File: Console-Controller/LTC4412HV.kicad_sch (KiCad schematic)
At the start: 5 parts, among them Q5 Si7463DP, U11 LTC4412HVIS6

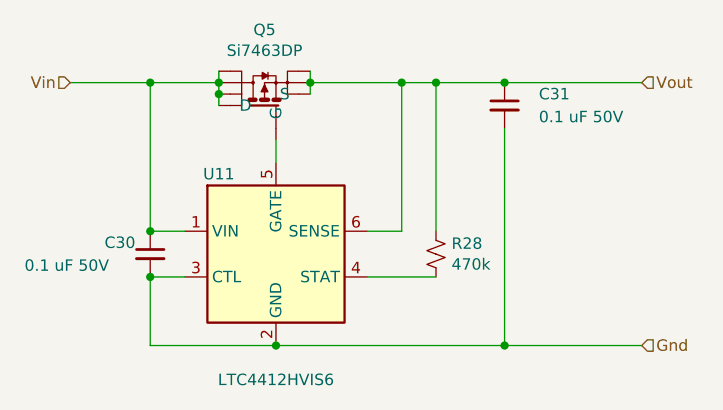
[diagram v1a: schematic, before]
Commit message: added polyfuse to LTC1760 output
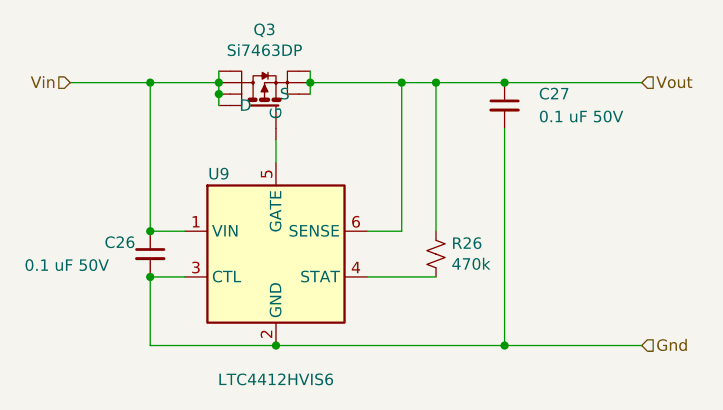
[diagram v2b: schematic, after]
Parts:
- renumbered C30 to C26, C31 to C27, Q5 to Q3, R28 to R26, U11 to U9
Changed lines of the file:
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@@
   (symbol (lib_id "Power_Management:LTC4412xS6") (at 140.97 101.6 0)
     (in_bom yes) (on_board yes)
-    (property "Reference" "U11" (id 0) (at 134.62 92.71 0))
+    (property "Reference" "U9" (id 0) (at 134.62 92.71 0))
     (property "Value" "LTC4412HVIS6" (id 1) (at 140.97 115.57 0))
     (property "Footprint" "Package_TO_SOT_SMD:TSOT-23-6" (id 2) (at 157.48 110.49 0)
@@
   (symbol (lib_id "ProjectDevices:Si7463DP") (at 139.7 82.55 270) (mirror x)
     (in_bom yes) (on_board yes)
-    (property "Reference" "Q5" (id 0) (at 139.7 76.6826 90))
+    (property "Reference" "Q3" (id 0) (at 139.7 76.6826 90))
     (property "Value" "Si7463DP" (id 1) (at 139.7 78.994 90))
     (property "Footprint" "Package_SO:PowerPAK_SO-8_Single" (id 2) (at 139.7 82.55 0)
@@
   (symbol (lib_id "Device:C_Small") (at 127 101.6 0)
     (in_bom yes) (on_board yes)
-    (property "Reference" "C30" (id 0) (at 121.92 100.33 0)
+    (property "Reference" "C26" (id 0) (at 121.92 100.33 0)
       (effects (font (size 1.27 1.27)) (justify left))
     )
@@
   (symbol (lib_id "Device:C_Small") (at 166.37 85.09 0)
     (in_bom yes) (on_board yes)
-    (property "Reference" "C31" (id 0) (at 170.18 83.82 0)
+    (property "Reference" "C27" (id 0) (at 170.18 83.82 0)
       (effects (font (size 1.27 1.27)) (justify left))
     )
@@
   (symbol (lib_id "Device:R_Small_US") (at 158.75 101.6 0)
     (in_bom yes) (on_board yes)
-    (property "Reference" "R28" (id 0) (at 160.4772 100.4316 0)
+    (property "Reference" "R26" (id 0) (at 160.4772 100.4316 0)
       (effects (font (size 1.27 1.27)) (justify left))
     )

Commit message: latest WIP, LTC1760 module ready for layout, strone-controller ready for layout but needs mech board drawings
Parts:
- renumbered C26 to C?, C27 to C?, Q3 to Q?, R26 to R?, U9 to U?
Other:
- company: Guatek -> (none)
- title: WW-Battery-Pack PCBs -> Console-Controller
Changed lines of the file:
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@@
   (paper "A4")
   (title_block
-    (title "WW-Battery-Pack PCBs")
-    (date "2020-07-27")
+    (title "Console-Controller")
+    (date "2022-12-15")
     (rev "A")
-    (company "Guatek")
     (comment 1 "First version of 6-pack board stack for Inspired Energy NH2034HD34")
   )
@@
   (symbol (lib_id "Power_Management:LTC4412xS6") (at 140.97 101.6 0)
     (in_bom yes) (on_board yes)
-    (property "Reference" "U9" (id 0) (at 134.62 92.71 0))
+    (property "Reference" "U?" (id 0) (at 134.62 92.71 0))
     (property "Value" "LTC4412HVIS6" (id 1) (at 140.97 115.57 0))
     (property "Footprint" "Package_TO_SOT_SMD:TSOT-23-6" (id 2) (at 157.48 110.49 0)
@@
   (symbol (lib_id "ProjectDevices:Si7463DP") (at 139.7 82.55 270) (mirror x)
     (in_bom yes) (on_board yes)
-    (property "Reference" "Q3" (id 0) (at 139.7 76.6826 90))
+    (property "Reference" "Q?" (id 0) (at 139.7 76.6826 90))
     (property "Value" "Si7463DP" (id 1) (at 139.7 78.994 90))
     (property "Footprint" "Package_SO:PowerPAK_SO-8_Single" (id 2) (at 139.7 82.55 0)
@@
   (symbol (lib_id "Device:C_Small") (at 127 101.6 0)
     (in_bom yes) (on_board yes)
-    (property "Reference" "C26" (id 0) (at 121.92 100.33 0)
+    (property "Reference" "C?" (id 0) (at 121.92 100.33 0)
       (effects (font (size 1.27 1.27)) (justify left))
     )
@@
   (symbol (lib_id "Device:C_Small") (at 166.37 85.09 0)
     (in_bom yes) (on_board yes)
-    (property "Reference" "C27" (id 0) (at 170.18 83.82 0)
+    (property "Reference" "C?" (id 0) (at 170.18 83.82 0)
       (effects (font (size 1.27 1.27)) (justify left))
     )
@@
   (symbol (lib_id "Device:R_Small_US") (at 158.75 101.6 0)
     (in_bom yes) (on_board yes)
-    (property "Reference" "R26" (id 0) (at 160.4772 100.4316 0)
-      (effects (font (size 1.27 1.27)) (justify left))
-    )
+    (property "Reference" "R?" (id 0) (at 160.4772 100.4316 0)
+      (effects (font (size 1.27 1.27)) (justify left))
+    )
